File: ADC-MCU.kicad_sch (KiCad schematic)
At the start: 43 parts, among them J1 2171790001, J3 Conn_01x04_Pin, SW1 SW_Push, SW2 SW_Push, U1 OPA2140AIDR, U2 CD4052BPWR, U3 LM393DR, U4 ADG601BRMZ-REEL7, U5 ESP32-C3-WROOM-02-N4, U6 AP2112K-3.3, U7 MCP601T-E_OT

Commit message: pcb layout draft
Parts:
- C1: footprint Capacitor_SMD:C_1812_4532Metric -> footprints_pretty:0805_cap_nosilk
- C11, C12, C13, C16, C2, C4, C5, C6, C7, C8: footprint Capacitor_SMD:C_0805_2012Metric -> footprints_pretty:0805_cap_nosilk
- R1, R10, R15, R16, R17, R18, R19, R2, R24, R3, R4, R5, R6, R7, R9: footprint Resistor_SMD:R_0805_2012Metric -> footprints_pretty:res_0805_nosilk
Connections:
- net 3V3 is gone; now on net +3V3: C12.2, C13.2, J3.1 (Pin_1), R17.2, R18.2, R19.2, R24.2, U5.1 (3V3)

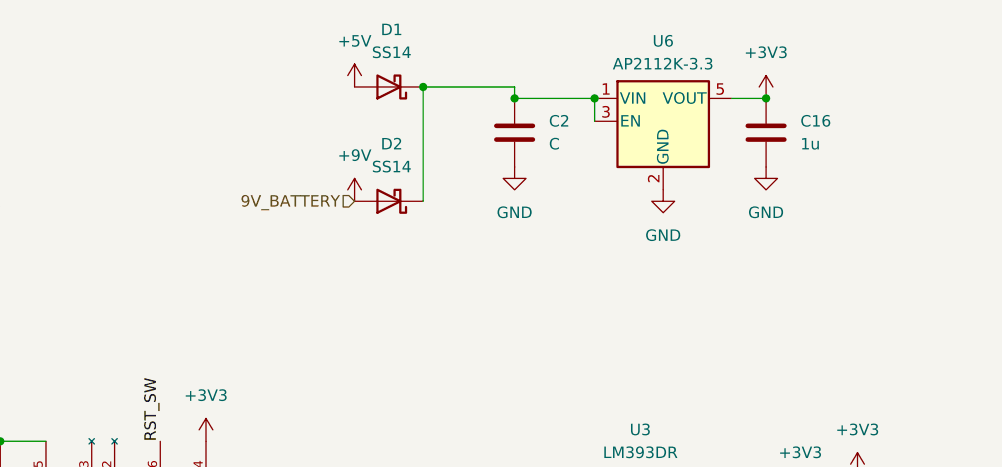
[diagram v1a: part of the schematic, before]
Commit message: fixed drc errors
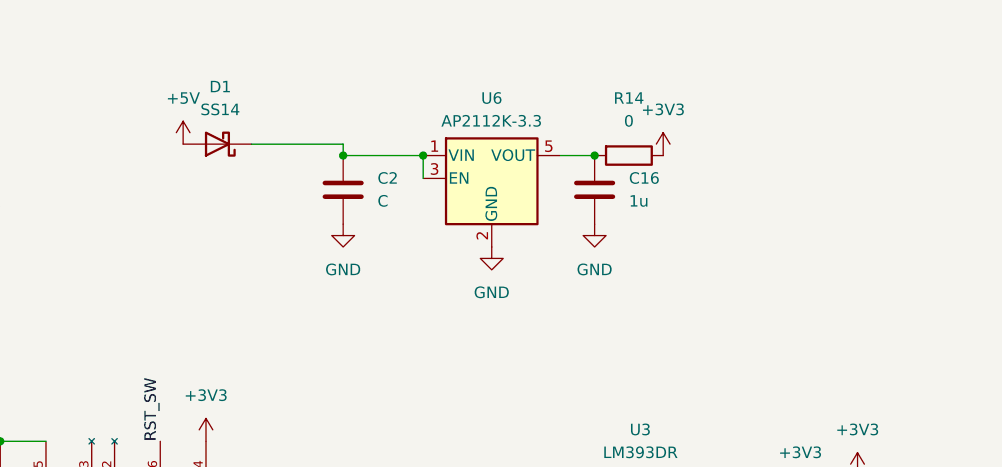
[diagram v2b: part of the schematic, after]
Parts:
- removed D2: SS14, Diode_SMD:D_SMA, symbol Diode:SS14
- added R14: 0, Resistor_SMD:R_0805_2012Metric, symbol Device:R
- C16, C2: footprint footprints_pretty:0805_cap_nosilk -> Capacitor_SMD:C_0805_2012Metric
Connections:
- net +3V3: now also R14.1; no longer C16.2, U6.5 (VOUT)
- new net: C16.2, R14.2, U6.5 (VOUT)
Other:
- moved on the sheet: C16, C2, D1, U6

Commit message: updated components
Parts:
- removed U2: CD4052BPWR, footprints:PW0016A_N, symbol CD4052BPWR:CD4052BPWR
- removed U4: ADG601BRMZ-REEL7, ADG601BRMZ-REEL7:SOP65P490X110-8N, symbol ADG601BRMZ-REEL7:ADG601BRMZ-REEL7
- added U13: 74HC4052PW_118, TSSOP16_5P1X4P5_NEX, symbol capstone:74HC4052PW_118
- added U2: ADG701LBRJZ-REEL7, footprints:RJ_5_ADI, symbol capstone:ADG701LBRJZ-REEL7
- C1: footprint footprints_pretty:0805_cap_nosilk -> Resistor_SMD:R_1812_4532Metric
- U1: value OPA2140AIDR -> OPA2333AIDR; footprint footprints:D8 -> Package_SO:SOIC-8_5.3x5.3mm_P1.27mm
- renumbered R14 to R102
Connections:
- net +3V3: now also U13.12 (1Y0), U13.16 (VCC), U2.5 (VDD)
- net -VREF: now also U13.4 (2Y3)
- net 1.65V: now also U13.1 (2Y0)
- net DS_ADC: now also U13.2 (2Y2)
- net GND: now also U13.11 (1Y3), U13.14 (1Y1), U13.15 (1Y2), U13.6 (*E), U13.7 (VEE), U13.8 (GND), U2.3 (GND)
- net MUX_A: now also U13.10 (S0)
- net MUX_B: now also U13.9 (S1)
- net RST_SW: now also U13.13 (1Z), U2.4 (IN)
- net V_BG: now also U13.5 (2Y1)
- net S: now reaches C1.1, R1.2, U1.2 (INA-)
- net S: now also U2.2 (S)
- net D: now reaches C1.2, TP5.1, U1.1 (OUTA), U3.3 (1IN+), U3.6 (2IN-)
- net D: now also U2.1 (D)
- net Integrator_In: now reaches R1.1
- net Integrator_In: now also U13.3 (2Z)

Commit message: moved more things
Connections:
- net ADC_IN2: now also U5.18 (IO0); no longer U5.17 (IO1)
- net ESP_ADC_1: now also U5.17 (IO1); no longer U5.18 (IO0)
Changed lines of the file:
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@@
+		)
+	)
+	(label "ESP_ADC_1"
+		(at 220.98 74.93 180)
+		(effects
+			(font
+				(size 1.27 1.27)
+			)
+			(justify right bottom)
 		)
 	)
@@
 		)
 	)
-	(label "ESP_ADC_1"
-		(at 220.98 72.39 180)
-		(effects
-			(font
-				(size 1.27 1.27)
-			)
-			(justify right bottom)
-		)
-	)
 	(label "USB_D+"
 		(at 259.08 27.94 0)
@@
 	(label "S"
 		(at 21.59 76.2 180)
+		(effects
+			(font
+				(size 1.27 1.27)
+			)
+			(justify right bottom)
+		)
+	)
+	(label "ESP_ADC_2"
+		(at 220.98 72.39 180)
 		(effects
 			(font
@@
 		(effects
 			(font
-				(size 1.27 1.27)
-			)
-			(justify right bottom)
-		)
-	)
-	(label "ESP_ADC_2"
-		(at 220.98 74.93 180)
-		(effects
-			(font
